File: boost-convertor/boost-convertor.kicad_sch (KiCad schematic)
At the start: 35 parts, among them J2 Screw_Terminal_01x02, J3 AVR-ISP-6, J4 TYPE-C 6P, U1 ATMEGA328P-AU, U2 MC34063ECN, U3 ADS1115IDGSR, U4 MAX7219, Y1 Crystal

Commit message: fix bugs
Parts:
- J3: footprint (none) -> footprint:AVR-4pin
- L1: value 68uH -> 100uH
- R4: value 120k -> 146.7k
- R5: value 25k -> 16.7k
- U4: footprint footprint:TQFP32_32A_MCH -> footprint:DGS0010A_L
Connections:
- net PGND is gone; now on net GND: C1.2, C3.2, J2.2 (Pin_2), U2.2 (SWE), U2.4 (GND), U4.4 (GND), U4.9 (GND)
- net SGND is gone; now on net GND: C2.2, R3.1, U3.1 (ADDR), U3.3 (GND)
- net MOSI: now also J3.2 (MOSI); no longer J3.4 (MOSI)
- net RESET: now also J3.4 (~{RST}); no longer J3.5 (~{RST})
- no-connect marks 27 -> 25
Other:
- title: (none) -> boost convertor 
- moved on the sheet: J4, R1, R11, R12, R13, R8

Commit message: complete layout
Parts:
- J3: footprint footprint:AVR-4pin -> footprint:AVR-5pin
- U4: footprint footprint:DGS0010A_L -> footprint:SSOP-24
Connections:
- net GND: now also J3.5 (GND)
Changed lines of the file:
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@@
 	(wire
 		(pts
-			(xy 166.37 163.83) (xy 170.18 163.83)
+			(xy 158.75 165.1) (xy 165.1 165.1)
 		)
 		(stroke
@@
 	(wire
 		(pts
-			(xy 166.37 166.37) (xy 170.18 166.37)
+			(xy 158.75 167.64) (xy 165.1 167.64)
 		)
 		(stroke
@@
 	(wire
 		(pts
+			(xy 163.83 175.26) (xy 163.83 179.07)
+		)
+		(stroke
+			(width 0)
+			(type default)
+		)
+	)
+	(wire
+		(pts
 			(xy 68.58 158.75) (xy 82.55 158.75)
 		)
@@
 	(wire
 		(pts
-			(xy 166.37 171.45) (xy 170.18 171.45)
+			(xy 158.75 172.72) (xy 165.1 172.72)
 		)
 		(stroke
@@
 	(wire
 		(pts
-			(xy 166.37 168.91) (xy 170.18 168.91)
+			(xy 158.75 175.26) (xy 163.83 175.26)
+		)
+		(stroke
+			(width 0)
+			(type default)
+		)
+	)
+	(wire
+		(pts
+			(xy 158.75 170.18) (xy 165.1 170.18)
 		)
 		(stroke
@@
 	)
 	(label "MISO"
-		(at 170.18 163.83 0)
+		(at 165.1 165.1 0)
 		(effects
 			(font
@@
 	)
 	(label "SCK"
-		(at 170.18 168.91 0)
+		(at 165.1 170.18 0)
 		(effects
 			(font
@@
 	)
 	(label "RESET"
-		(at 170.18 171.45 0)
+		(at 165.1 172.72 0)
 		(effects
 			(font
@@
 	)
 	(label "MOSI"
-		(at 170.18 166.37 0)
+		(at 165.1 167.64 0)
 		(effects
 			(font
@@
 	(symbol
 		(lib_id "Connector:AVR-ISP-6")
-		(at 156.21 168.91 0)
+		(at 148.59 170.18 0)
 		(unit 1)
 		(exclude_from_sim no)
@@
 		(on_board yes)
 		(dnp no)
-		(fields_autoplaced yes)
 		(property "Reference" "J3"
-			(at 147.32 166.3699 0)
+			(at 146.05 169.672 0)
 			(effects
 				(font
@@
 		)
 		(property "Value" "AVR-ISP-6"
-			(at 147.32 168.9099 0)
+			(at 152.654 163.576 0)
 			(effects
 				(font
@@
 			)
 		)
-		(property "Footprint" "footprint:AVR-4pin"
-			(at 149.86 167.64 90)
+		(property "Footprint" "footprint:AVR-5pin"
+			(at 142.24 168.91 90)
 			(effects
 				(font
@@
 		)
 		(property "Datasheet" "~"
-			(at 123.825 182.88 0)
+			(at 116.205 184.15 0)
 			(effects
 				(font
@@
 		)
 		(property "Description" "Atmel 6-pin ISP connector"
-			(at 156.21 168.91 0)
+			(at 148.59 170.18 0)
 			(effects
 				(font
@@
 		(pin "3"
 		)
+		(pin "5"
+		)
 		(instances
 			(project ""
@@
 	)
 	(symbol
+		(lib_id "power:GND")
+		(at 163.83 179.07 0)
+		(unit 1)
+		(exclude_from_sim no)
+		(in_bom yes)
+		(on_board yes)
+		(dnp no)
+		(fields_autoplaced yes)
+		(property "Reference" "#PWR025"
+			(at 163.83 185.42 0)
+			(effects
+				(font
+					(size 1.27 1.27)
+				)
+				(hide yes)
+			)
+		)
+		(property "Value" "GND"
+			(at 163.83 184.15 0)
+			(effects
+				(font
+					(size 1.27 1.27)
+				)
+			)
+		)
+		(property "Footprint" ""
+			(at 163.83 179.07 0)
+			(effects
+				(font
+					(size 1.27 1.27)
+				)
+				(hide yes)
+			)
+		)
+		(property "Datasheet" ""
+			(at 163.83 179.07 0)
+			(effects
+				(font
+					(size 1.27 1.27)
+				)
+				(hide yes)
+			)
+		)
+		(property "Description" "Power symbol creates a global label with name \"GND\" , ground"
+			(at 163.83 179.07 0)
+			(effects
+				(font
+					(size 1.27 1.27)
+				)
+				(hide yes)
+			)
+		)
+		(pin "1"
+		)
+		(instances
+			(project ""
+				(path "/2978165a-4816-4cd6-bfe1-5d3d637e2db4"
+					(reference "#PWR025")
+					(unit 1)
+				)
+			)
+		)
+	)
+	(symbol
 		(lib_id "atmega328P:ATMEGA328P-AU")
 		(at 110.49 101.6 0)
@@
 		(lib_id "Device:C")
 		(at 85.09 120.65 0)
+		(mirror y)
 		(unit 1)
 		(exclude_from_sim no)
@@
 		(dnp no)
 		(property "Reference" "C7"
-			(at 80.772 119.38 0)
+			(at 89.408 119.38 0)
 			(effects
 				(font
@@
 		)
 		(property "Value" "0.1u"
-			(at 80.772 121.92 0)
+			(at 89.408 121.92 0)
 			(effects
 				(font
@@
 		)
 		(property "Footprint" "Capacitor_SMD:C_0603_1608Metric"
-			(at 86.0552 124.46 0)
+			(at 84.1248 124.46 0)
 			(effects
 				(font
@@
 		(on_board yes)
 		(dnp no)
-		(fields_autoplaced yes)
 		(property "Reference" "U2"
 			(at 105.41 26.67 0)
@@
 			)
 		)
-		(property "Footprint" "footprint:DGS0010A_L"
+		(property "Footprint" "footprint:SSOP-24"
 			(at 49.53 129.54 0)
 			(effects
@@
 		(on_board yes)
 		(dnp no)
-		(fields_autoplaced yes)
 		(property "Reference" "R3"
 			(at 68.58 54.6099 0)
@@
 		(on_board yes)
 		(dnp no)
-		(fields_autoplaced yes)
 		(property "Reference" "U3"
 			(at 233.68 96.52 0)

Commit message: The finnal pcb complete
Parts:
- C4, C5: value 0.1u -> 18pf
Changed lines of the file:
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@@
 			)
 		)
-		(property "Value" "0.1u"
+		(property "Value" "18pf"
 			(at 128.27 171.4499 0)
 			(effects
@@
 			)
 		)
-		(property "Value" "0.1u"
+		(property "Value" "18pf"
 			(at 115.57 171.4499 0)
 			(effects

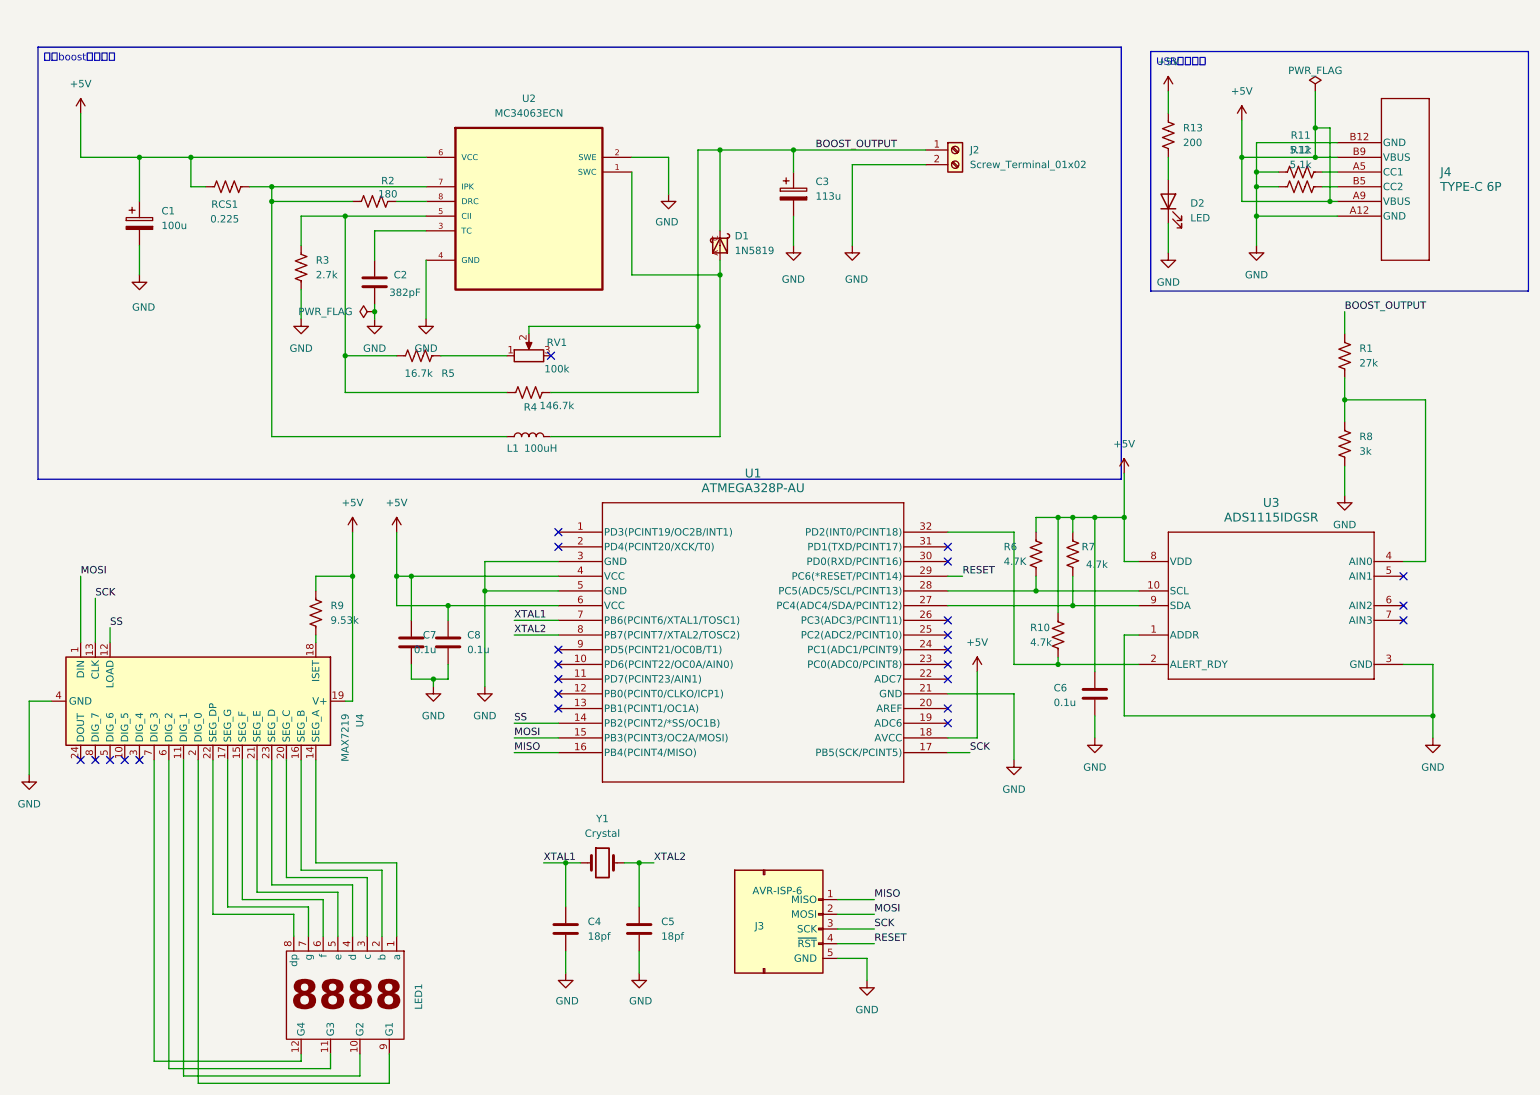
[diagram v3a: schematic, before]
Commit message: add a external mosfet improve ouput power
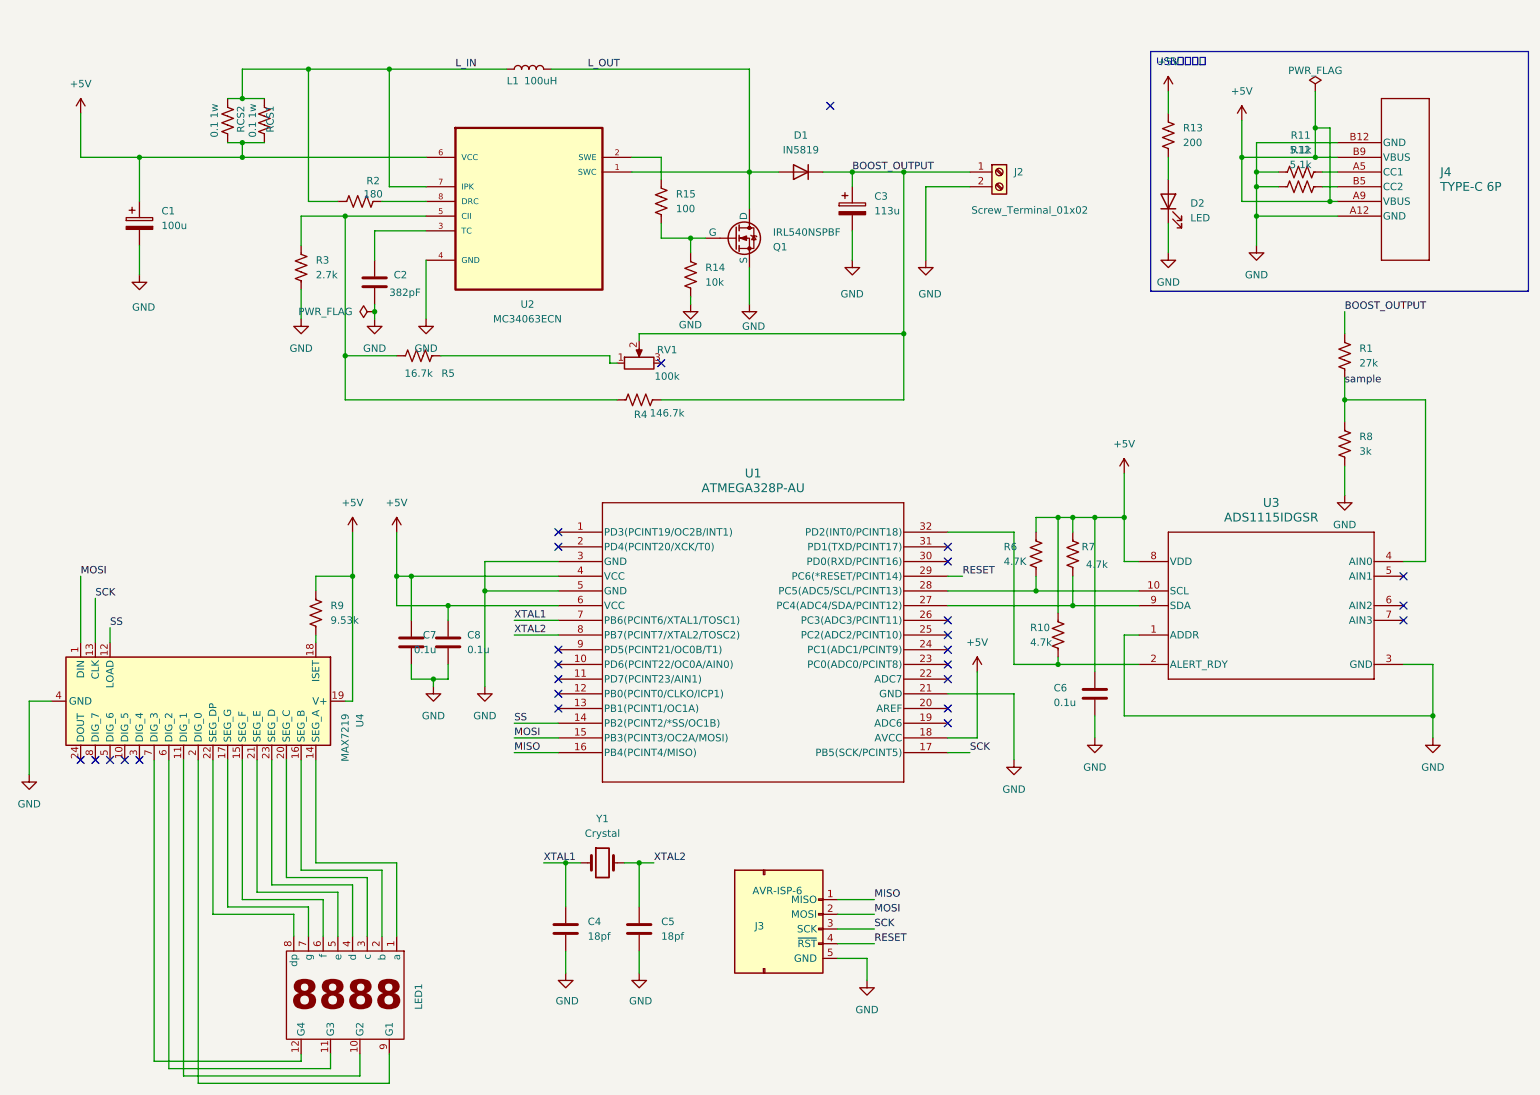
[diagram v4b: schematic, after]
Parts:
- removed D1: 1N5819, footprint:DO41-10, symbol Diode:1N5819
- added D1: IN5819, Diode_SMD:D_SMA, symbol Device:D
- added Q1: IRL540NSPBF, footprint:TO254P1524X483-3N, symbol Simulation_SPICE:NMOS
- added R14: 10k, Resistor_SMD:R_0603_1608Metric, symbol Device:R_US
- added R15: 100, Resistor_SMD:R_0603_1608Metric, symbol Device:R_US
- added RCS2: 0.1 1w, Resistor_SMD:R_1206_3216Metric, symbol Device:R_US
- RCS1: value 0.225 -> 0.1 1w; footprint Resistor_SMD:R_0603_1608Metric -> Resistor_SMD:R_1206_3216Metric
- U4: footprint footprint:SSOP-24 -> Package_SO:SOP-24_7.5x15.4mm_P1.27mm
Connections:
- net +5V: now also RCS2.1
- net BOOST_OUTPUT: now also D1.1 (K)
- net GND: now also Q1.3 (S), R14.2; no longer U2.2 (SWE)
- net L_OUT: now reaches L1.2, U2.1 (SWC)
- net L_OUT: now also D1.2 (A), Q1.1 (D)
- net sample: now reaches R1.2, R8.1, U3.4 (AIN0)
- net L_IN: now reaches L1.1, R2.1, RCS1.2, U2.7 (IPK)
- net L_IN: now also RCS2.2
- new net: Q1.2 (G), R14.1, R15.2
- new net: R15.1, U2.2 (SWE)
- no-connect marks 25 -> 26
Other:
- moved on the sheet: C3, J2, L1, R2, R4, RCS1, RV1
